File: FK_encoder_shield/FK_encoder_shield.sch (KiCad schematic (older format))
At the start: 5 parts, among them J1 molex-35363-0660, J2 Conn_01x05_Female

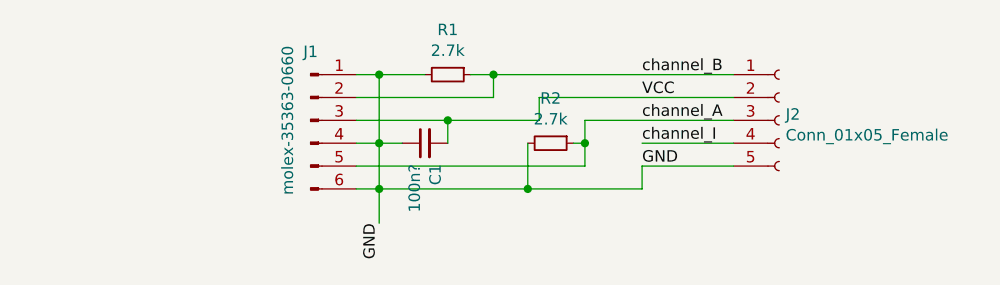
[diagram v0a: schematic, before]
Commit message: replace conn symbol on encoder shield
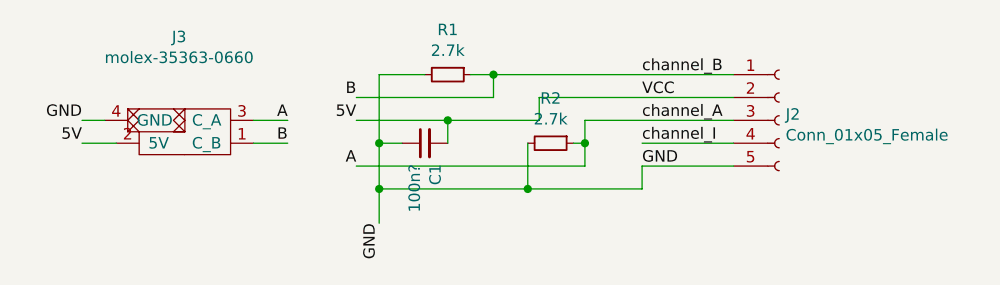
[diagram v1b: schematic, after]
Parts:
- removed J1: molex-35363-0660, FK_connectors:molex-35363-0660, symbol Connector:Conn_01x06_Male
- added J3: molex-35363-0660, FK_connectors:molex-35363-0660, symbol FK_fpga_shield_custom_symbols:molex-35363-0660
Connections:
- net GND: now also J3.4 (GND)
- net VCC renamed 5V
- net 5V: now also J3.2 (5V)
- net channel_A renamed A
- net A: now also J3.3 (C_A)
- net channel_B renamed B
- net B: now also J3.1 (C_B)
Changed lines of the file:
@@
 	6400 3750 6000 3750
-$Comp
-L Connector:Conn_01x06_Male J1
-U 1 1 6037CC3D
-P 4550 3650
-F 0 "J1" H 4550 3950 50  0000 C CNN
-F 1 "molex-35363-0660" V 4450 3650 50  0000 C CNN
-F 2 "FK_connectors:molex-35363-0660" H 4550 3650 50  0001 C CNN
-F 3 "~" H 4550 3650 50  0001 C CNN
-	1    4550 3650
-	1    0    0    -1
-$EndComp
 $Comp
 L Device:R_Small R1
@@
 GND
 Wire Wire Line
-	4750 3950 4850 3950
-Wire Wire Line
-	4750 3750 4850 3750
-Wire Wire Line
 	4850 3750 4850 3950
-Wire Wire Line
-	4750 3450 4850 3450
 Wire Wire Line
 	4850 3450 4850 3750
@@
 	5350 3450 5350 3550
 Wire Wire Line
-	5350 3550 4750 3550
-Wire Wire Line
 	5350 3450 6400 3450
 Wire Wire Line
 	5750 3650 5750 3750
-Wire Wire Line
-	5750 3850 4750 3850
 Wire Wire Line
 	5550 3550 5550 3650
@@
 Wire Wire Line
 	5050 3450 4850 3450
-Connection ~ 4850 3450
 $Comp
 L Device:C_Small C1
@@
 	0    -1   -1   0
 $EndComp
+$Comp
+L FK_fpga_shield_custom_symbols:molex-35363-0660 J3
+U 1 1 603A634D
+P 4000 3700
+F 0 "J3" H 3975 4115 50  0000 C CNN
+F 1 "molex-35363-0660" H 3975 4024 50  0000 C CNN
+F 2 "FK_connectors:molex-35363-0660" H 4250 3700 50  0001 C CNN
+F 3 "" H 4250 3700 50  0001 C CNN
+	1    4000 3700
+	1    0    0    -1
+$EndComp
+Wire Wire Line
+	5750 3850 4750 3850
+Wire Wire Line
+	5350 3550 4750 3550
+Text Label 4750 3550 2    50   ~ 0
+B
+Text Label 4750 3850 2    50   ~ 0
+A
+Text Label 4750 3650 2    50   ~ 0
+5V
+Text Label 3550 3650 2    50   ~ 0
+GND
+Text Label 3550 3750 2    50   ~ 0
+5V
+Wire Wire Line
+	3550 3750 3700 3750
+Wire Wire Line
+	3650 3650 3550 3650
+Text Label 4450 3750 2    50   ~ 0
+B
+Text Label 4450 3650 2    50   ~ 0
+A
+Wire Wire Line
+	4450 3650 4300 3650
+Wire Wire Line
+	4450 3750 4300 3750
 $EndSCHEMATC

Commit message: change connector to microclasp 4 wire
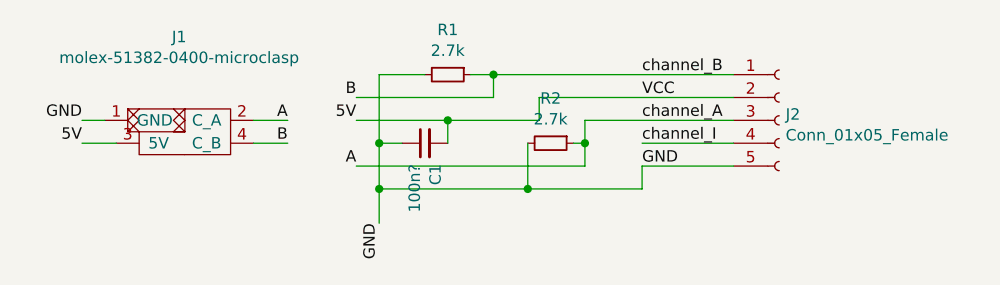
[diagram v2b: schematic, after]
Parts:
- removed J3: molex-35363-0660, FK_connectors:molex-35363-0660, symbol FK_fpga_shield_custom_symbols:molex-35363-0660
- added J1: molex-51382-0400-microclasp, FK_connectors:Molex_MicroClasp_55935-0410_1x04_P2.00mm_Horizontal_3DMODEL, symbol FK_fpga_shield_custom_symbols:molex-51382-0400-microclasp
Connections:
- net 5V: now also J1.3 (5V)
- net A: now also J1.2 (C_A)
- net B: now also J1.4 (C_B)
- net GND: now also J1.1 (GND)
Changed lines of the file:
@@
 	0    -1   -1   0
-$EndComp
-$Comp
-L FK_fpga_shield_custom_symbols:molex-35363-0660 J3
-U 1 1 603A634D
-P 4000 3700
-F 0 "J3" H 3975 4115 50  0000 C CNN
-F 1 "molex-35363-0660" H 3975 4024 50  0000 C CNN
-F 2 "FK_connectors:molex-35363-0660" H 4250 3700 50  0001 C CNN
-F 3 "" H 4250 3700 50  0001 C CNN
-	1    4000 3700
-	1    0    0    -1
 $EndComp
 Wire Wire Line
@@
 Wire Wire Line
 	4450 3750 4300 3750
+$Comp
+L FK_fpga_shield_custom_symbols:molex-51382-0400-microclasp J1
+U 1 1 603CD8A1
+P 4000 3700
+F 0 "J1" H 3975 4115 50  0000 C CNN
+F 1 "molex-51382-0400-microclasp" H 3975 4024 50  0000 C CNN
+F 2 "FK_connectors:Molex_MicroClasp_55935-0410_1x04_P2.00mm_Horizontal_3DMODEL" H 4250 3700 50  0001 C CNN
+F 3 "" H 4250 3700 50  0001 C CNN
+	1    4000 3700
+	1    0    0    -1
+$EndComp
 $EndSCHEMATC
